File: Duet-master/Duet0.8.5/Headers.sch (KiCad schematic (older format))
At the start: 19 parts, among them J10 GND V_IN, J11 GND V_IN, J12 E1 TEMP, J13 Probe, J6 EXPANSION, J7 PanelDUE, J8 POWER IN, J9 5V_PS, U10 USB_3.0_Receptacle, U13 USB_3.0_Receptacle_4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

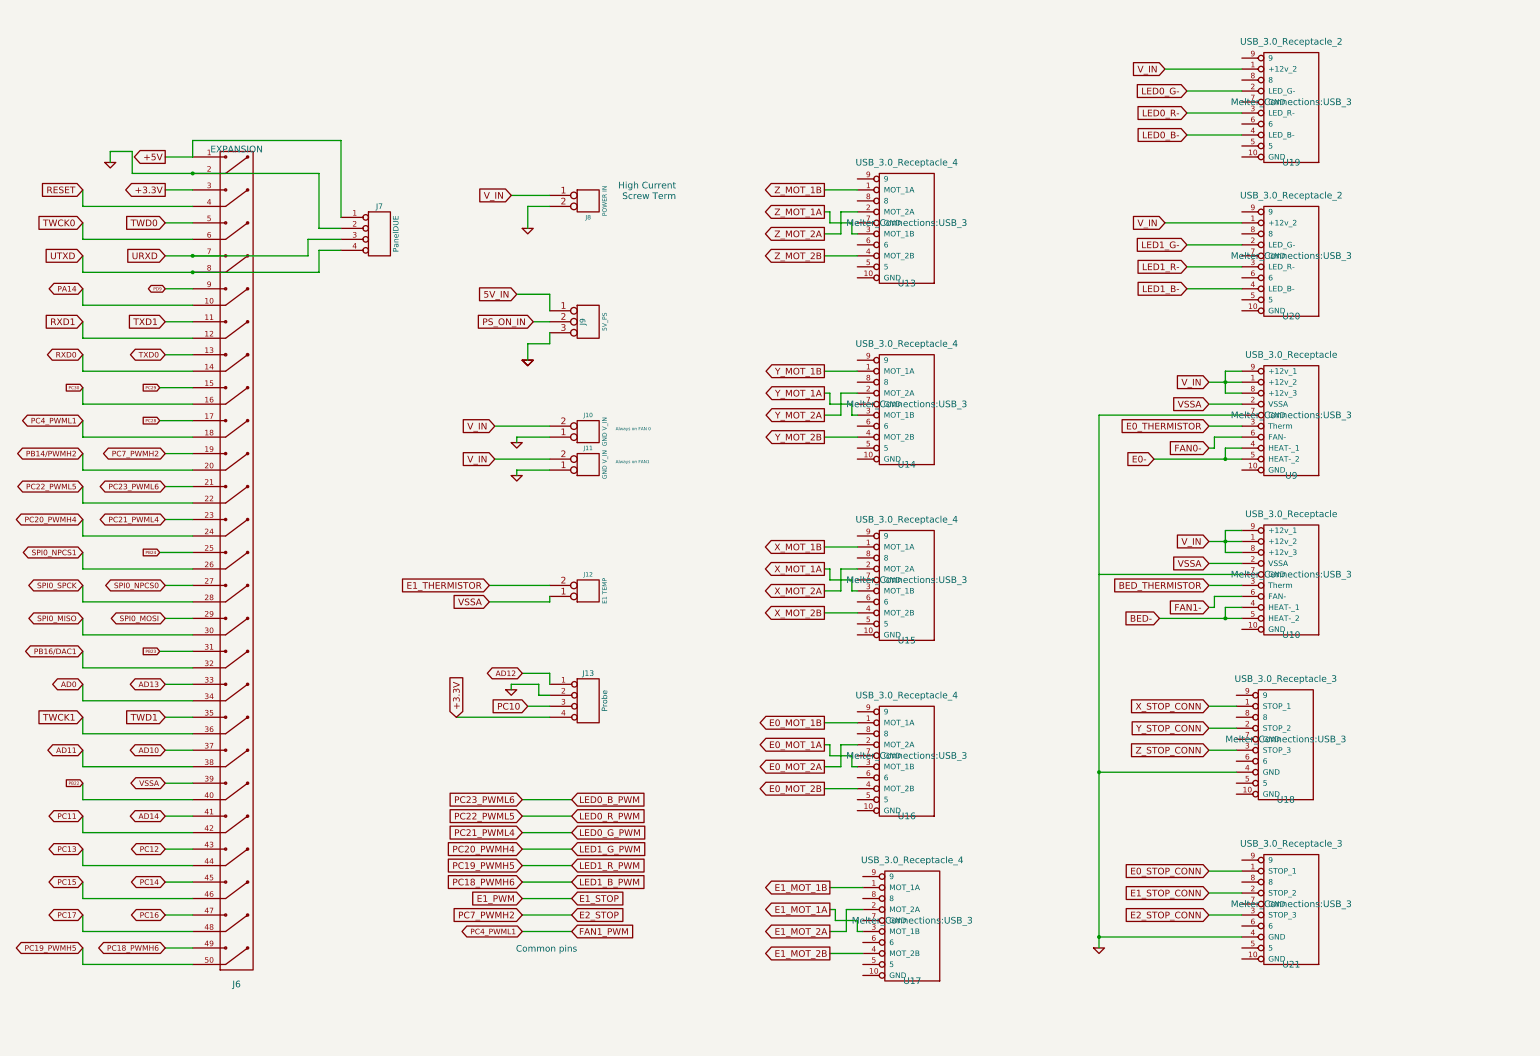
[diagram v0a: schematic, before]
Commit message: 0.1" headers added
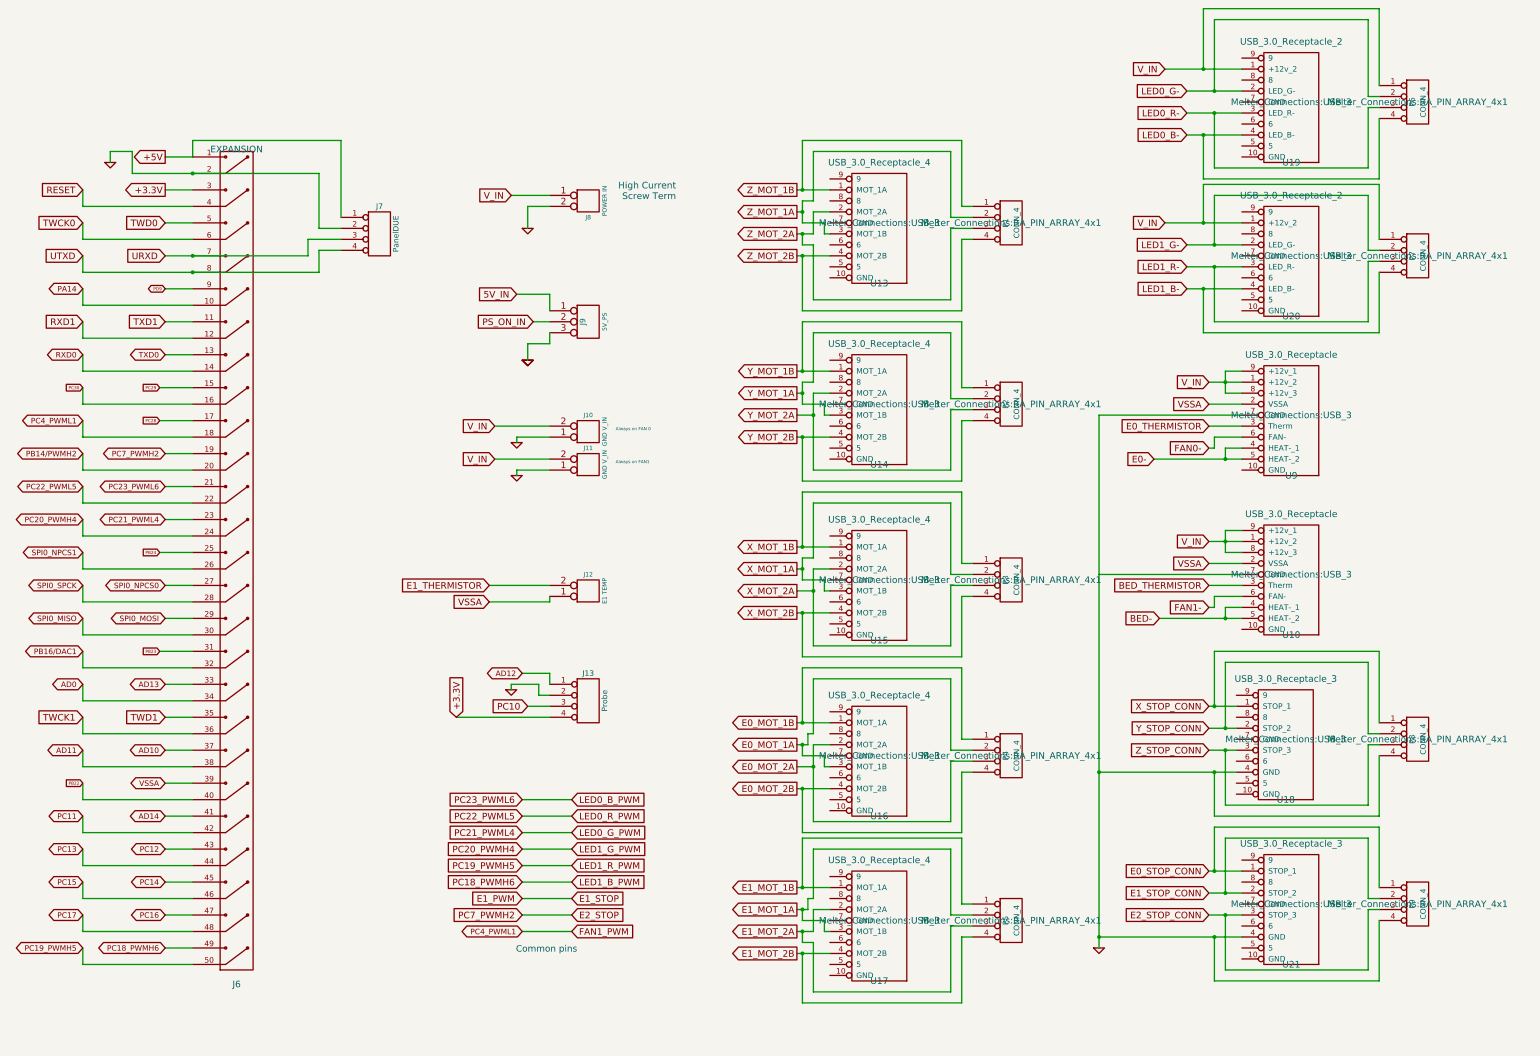
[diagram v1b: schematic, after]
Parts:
- added P1, P2, P3, P4, P5, P6, P7, P8, P9: CONN_4, Melter_Connections:RA_PIN_ARRAY_4x1, symbol CONN_4
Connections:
- net E0_MOT_1A: now also P4.2 (P2)
- net E0_MOT_1B: now also P4.1 (P1)
- net E0_MOT_2A: now also P4.3 (P3)
- net E0_MOT_2B: now also P4.4 (P4)
- net E0_STOP_CONN: now also P9.1 (P1)
- net E1_MOT_1A: now also P5.2 (P2)
- net E1_MOT_1B: now also P5.1 (P1)
- net E1_MOT_2A: now also P5.3 (P3)
- net E1_MOT_2B: now also P5.4 (P4)
- net E1_STOP_CONN: now also P9.2 (P2)
- net E2_STOP_CONN: now also P9.3 (P3)
- net GND: now also P8.4 (P4), P9.4 (P4)
- net LED0_B-: now also P6.4 (P4)
- net LED0_G-: now also P6.2 (P2)
- net LED0_R-: now also P6.3 (P3)
- net LED1_B-: now also P7.4 (P4)
- net LED1_G-: now also P7.2 (P2)
- net LED1_R-: now also P7.3 (P3)
- net V_IN: now also P6.1 (P1), P7.1 (P1)
- net X_MOT_1A: now also P3.2 (P2)
- net X_MOT_1B: now also P3.1 (P1)
- net X_MOT_2A: now also P3.3 (P3)
- net X_MOT_2B: now also P3.4 (P4)
- net X_STOP_CONN: now also P8.1 (P1)
- net Y_MOT_1A: now also P2.2 (P2)
- net Y_MOT_1B: now also P2.1 (P1)
- net Y_MOT_2A: now also P2.3 (P3)
- net Y_MOT_2B: now also P2.4 (P4)
- net Y_STOP_CONN: now also P8.2 (P2)
- net Z_MOT_1A: now also P1.2 (P2)
- net Z_MOT_1B: now also P1.1 (P1)
- net Z_MOT_2A: now also P1.3 (P3)
- net Z_MOT_2B: now also P1.4 (P4)
- net Z_STOP_CONN: now also P8.3 (P3)
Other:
- moved on the sheet: U13, U14, U15, U16, U17

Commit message: Routing started
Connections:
- net GND: now also U10.7 (GND)
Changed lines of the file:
@@
 AD12
 $Comp
-L GND #PWR32
+L GND #PWR028
 U 1 1 53B0339C
 P 6600 2750
-F 0 "#PWR32" H 6600 2750 30  0001 C CNN
+F 0 "#PWR028" H 6600 2750 30  0001 C CNN
 F 1 "GND" H 6600 2680 30  0001 C CNN
 F 2 "" H 6600 2750 60  0001 C CNN
@@
 $EndComp
 $Comp
-L GND #PWR29
+L GND #PWR029
 U 1 1 53B0339B
 P 6450 6950
-F 0 "#PWR29" H 6450 6950 30  0001 C CNN
+F 0 "#PWR029" H 6450 6950 30  0001 C CNN
 F 1 "GND" H 6450 6880 30  0001 C CNN
 F 2 "" H 6450 6950 60  0001 C CNN
@@
 $EndComp
 $Comp
-L GND #PWR34
+L GND #PWR030
 U 1 1 53B03391
 P 6600 3950
-F 0 "#PWR34" H 6600 3950 30  0001 C CNN
+F 0 "#PWR030" H 6600 3950 30  0001 C CNN
 F 1 "GND" H 6600 3880 30  0001 C CNN
 F 2 "" H 6600 3950 60  0001 C CNN
@@
 VSSA
 $Comp
-L GND #PWR33
+L GND #PWR031
 U 1 1 50885A83
 P 6600 3950
-F 0 "#PWR33" H 6600 3950 30  0001 C CNN
+F 0 "#PWR031" H 6600 3950 30  0001 C CNN
 F 1 "GND" H 6600 3880 30  0001 C CNN
 F 2 "" H 6600 3950 60  0001 C CNN
@@
 $EndComp
 $Comp
-L GND #PWR28
+L GND #PWR032
 U 1 1 5064C39B
 P 2800 2150
-F 0 "#PWR28" H 2800 2150 30  0001 C CNN
+F 0 "#PWR032" H 2800 2150 30  0001 C CNN
 F 1 "GND" H 2800 2080 30  0001 C CNN
 F 2 "" H 2800 2150 60  0001 C CNN
@@
 $EndComp
 $Comp
-L GND #PWR31
+L GND #PWR033
 U 1 1 556996C5
 P 6500 5000
-F 0 "#PWR31" H 6500 5000 30  0001 C CNN
+F 0 "#PWR033" H 6500 5000 30  0001 C CNN
 F 1 "GND" H 6500 4930 30  0001 C CNN
 F 2 "" H 6500 5000 60  0001 C CNN
@@
 V_IN
 $Comp
-L GND #PWR35
+L GND #PWR034
 U 1 1 55CB52F9
 P 11800 9300
-F 0 "#PWR35" H 11800 9300 30  0001 C CNN
+F 0 "#PWR034" H 11800 9300 30  0001 C CNN
 F 1 "GND" H 11800 9230 30  0001 C CNN
 F 2 "" H 11800 9300 60  0001 C CNN
@@
 $EndComp
 $Comp
-L GND #PWR30
+L GND #PWR035
 U 1 1 55C8CC85
 P 6500 4700
-F 0 "#PWR30" H 6500 4700 30  0001 C CNN
+F 0 "#PWR035" H 6500 4700 30  0001 C CNN
 F 1 "GND" H 6500 4630 30  0001 C CNN
 F 2 "" H 6500 4700 60  0001 C CNN
@@
 Wire Wire Line
 	13100 6000 12800 6000
-Wire Wire Line
-	11800 5900 13100 5900
 Connection ~ 12950 5600
 Wire Wire Line
@@
 	14350 9600 14350 9050
 Connection ~ 12850 9200
+Wire Wire Line
+	13100 5900 11800 5900
+Connection ~ 11800 5900
 $EndSCHEMATC

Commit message: More routing, even under crystals.
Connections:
- net LED0_B_PWM: no longer J6.21
- net LED0_G_PWM: no longer J6.23
- net LED0_R_PWM: no longer J6.22
- net LED1_B_PWM: no longer J6.49
- net LED1_G_PWM: no longer J6.24
- net LED1_R_PWM: no longer J6.50
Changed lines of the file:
@@
 	3300 3900 3550 3900
-Wire Wire Line
-	2550 9450 3550 9450
 Wire Wire Line
 	2550 7650 3550 7650
@@
 Wire Wire Line
 	3300 6000 3550 6000
-Wire Wire Line
-	3300 5400 3550 5400
-Wire Wire Line
-	3300 5100 3550 5100
 Wire Wire Line
 	3300 4800 3550 4800
@@
 	2550 4950 3550 4950
 Wire Wire Line
-	2550 5250 3550 5250
-Wire Wire Line
-	2550 5550 3550 5550
-Wire Wire Line
 	2550 5850 3550 5850
 Wire Wire Line
@@
 	3300 7500 3550 7500
 Wire Wire Line
-	3300 9300 3550 9300
-Wire Wire Line
 	2550 7050 3550 7050

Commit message: More routing
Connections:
- net E2_STOP: no longer J6.19
- net FAN1_PWM: no longer J6.18
- new net PC4_PWML1: J6.18
- new net PC7_PWMH2: J6.19
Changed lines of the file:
@@
 Text GLabel 6550 8850 0    60   Input ~ 0
 E1_PWM
-Text GLabel 7000 8850 2    60   Input ~ 0
-E1_STOP
 Text GLabel 7000 9000 2    60   Input ~ 0
 E2_STOP
@@
 	6800 4650 6500 4650
 Wire Wire Line
-	7000 9000 6550 9000
-Wire Wire Line
-	7000 8850 6550 8850
-Wire Wire Line
 	11800 4450 11800 9300
 Wire Wire Line
@@
 	3550 5700 3250 5700
 Wire Wire Line
-	7000 9150 6550 9150
-Wire Wire Line
 	2550 4350 3550 4350
 Wire Wire Line
@@
 	13100 5900 11800 5900
 Connection ~ 11800 5900
+Text GLabel 7000 8850 2    60   Input ~ 0
+E1_STOP
 $EndSCHEMATC

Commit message: Clean up
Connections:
- net GND: now also U10.10 (GND), U13.10 (GND), U14.10 (GND), U15.10 (GND), U16.10 (GND), U17.10 (GND), U18.10 (GND), U19.10 (GND), U20.10 (GND), U21.10 (GND), U9.10 (GND)
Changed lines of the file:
@@
 L GND #PWR034
 U 1 1 55CB52F9
-P 11800 9300
-F 0 "#PWR034" H 11800 9300 30  0001 C CNN
-F 1 "GND" H 11800 9230 30  0001 C CNN
-F 2 "" H 11800 9300 60  0001 C CNN
-F 3 "" H 11800 9300 60  0001 C CNN
-	1    11800 9300
+P 11800 9550
+F 0 "#PWR034" H 11800 9550 30  0001 C CNN
+F 1 "GND" H 11800 9480 30  0001 C CNN
+F 2 "" H 11800 9550 60  0001 C CNN
+F 3 "" H 11800 9550 60  0001 C CNN
+	1    11800 9550
 	1    0    0    -1
 $EndComp
@@
 	9100 5850 9050 5850
 Wire Wire Line
-	9100 5950 9100 5750
+	9100 5750 9100 5950
 Wire Wire Line
 	9050 5650 9350 5650
 Wire Wire Line
-	9300 5950 9100 5950
-Wire Wire Line
-	9300 6050 9300 5950
+	9100 5950 9300 5950
+Wire Wire Line
+	9300 5950 9300 6050
 Wire Wire Line
 	9300 6050 9350 6050
@@
 	9100 4250 9050 4250
 Wire Wire Line
-	9100 4350 9100 4150
+	9100 4150 9100 4350
 Wire Wire Line
 	9050 4050 9350 4050
 Wire Wire Line
-	9300 4350 9100 4350
-Wire Wire Line
-	9300 4450 9300 4350
+	9100 4350 9300 4350
+Wire Wire Line
+	9300 4350 9300 4450
 Wire Wire Line
 	9300 4450 9350 4450
@@
 	9050 2400 9350 2400
 Wire Wire Line
-	9300 2700 9100 2700
-Wire Wire Line
-	9300 2800 9300 2700
+	9100 2700 9300 2700
+Wire Wire Line
+	9300 2700 9300 2800
 Wire Wire Line
 	9300 2800 9350 2800
@@
 Connection ~ 11800 7700
 Wire Wire Line
-	13050 7700 11800 7700
-Wire Wire Line
-	13050 7500 12800 7500
-Wire Wire Line
-	13050 7300 12800 7300
-Wire Wire Line
-	13050 7100 12800 7100
+	11800 7700 13050 7700
+Wire Wire Line
+	12800 7500 13050 7500
+Wire Wire Line
+	12800 7300 13050 7300
+Wire Wire Line
+	12800 7100 13050 7100
 Connection ~ 11800 9200
 Wire Wire Line
-	13100 9200 11800 9200
-Wire Wire Line
-	13100 9000 12800 9000
-Wire Wire Line
-	13100 8800 12800 8800
-Wire Wire Line
-	13100 8600 12800 8600
-Wire Wire Line
-	13100 3300 12600 3300
-Wire Wire Line
-	13100 3100 12600 3100
-Wire Wire Line
-	13100 2900 12600 2900
-Wire Wire Line
-	13100 2700 12400 2700
-Wire Wire Line
-	13100 1500 12600 1500
-Wire Wire Line
-	13100 1300 12400 1300
+	11800 9200 13100 9200
+Wire Wire Line
+	12800 9000 13100 9000
+Wire Wire Line
+	12800 8800 13100 8800
+Wire Wire Line
+	12800 8600 13100 8600
+Wire Wire Line
+	12600 3300 13100 3300
+Wire Wire Line
+	12600 3100 13100 3100
+Wire Wire Line
+	12600 2900 13100 2900
+Wire Wire Line
+	12400 2700 13100 2700
+Wire Wire Line
+	12600 1500 13100 1500
+Wire Wire Line
+	12400 1300 13100 1300
 Wire Wire Line
 	6500 4950 6500 5000
@@
 	6800 4650 6500 4650
 Wire Wire Line
-	11800 4450 11800 9300
-Wire Wire Line
 	6550 8700 7000 8700
 Wire Wire Line
@@
 	13100 4550 12800 4550
 Wire Wire Line
-	13100 4450 11800 4450
-Wire Wire Line
-	13100 1700 12600 1700
-Wire Wire Line
-	13100 1900 12600 1900
+	11800 4450 13100 4450
+Wire Wire Line
+	12600 1700 13100 1700
+Wire Wire Line
+	12600 1900 13100 1900
 Wire Wire Line
 	6600 2550 6600 2750
@@
 	9100 2600 9050 2600
 Wire Wire Line
-	9100 2700 9100 2500
+	9100 2500 9100 2700
 Wire Wire Line
 	2550 2550 2550 2400
@@
 Connection ~ 12850 9200
 Wire Wire Line
-	13100 5900 11800 5900
+	11800 5900 13100 5900
 Connection ~ 11800 5900
 Text GLabel 7000 8850 2    60   Input ~ 0
 E1_STOP
+Wire Wire Line
+	11450 9400 13100 9400
+Connection ~ 11800 9400
+Wire Wire Line
+	11800 7900 13050 7900
+Connection ~ 11800 7900
+Wire Wire Line
+	11800 6400 13100 6400
+Connection ~ 11800 6400
+Wire Wire Line
+	11800 4950 13100 4950
+Connection ~ 11800 4950
+Connection ~ 11800 4450
+Wire Wire Line
+	11800 2100 13100 2100
+Connection ~ 11800 2100
+Wire Wire Line
+	11800 3500 13100 3500
+Connection ~ 11800 3500
+Wire Wire Line
+	11800 2100 11800 9550
+Wire Wire Line
+	8350 2150 8350 10200
+Wire Wire Line
+	8350 10200 11450 10200
+Wire Wire Line
+	11450 10200 11450 9400
+Wire Wire Line
+	9350 3200 8350 3200
+Wire Wire Line
+	8350 3200 8350 3300
+Connection ~ 8350 3300
+Wire Wire Line
+	9350 4850 8350 4850
+Connection ~ 8350 4850
+Connection ~ 8350 3200
+Wire Wire Line
+	9350 6450 8350 6450
+Connection ~ 8350 6450
+Wire Wire Line
+	9350 8050 8350 8050
+Connection ~ 8350 8050
+Wire Wire Line
+	9350 9550 8350 9550
+Connection ~ 8350 9550
 $EndSCHEMATC
